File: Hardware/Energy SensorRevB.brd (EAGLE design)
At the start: 159 x 63 mm, 42 parts, among them IC1 7805, IC2 ATMega328p-pu, IC3 ld33v, Q1 16MHz, X1 MAINS IN, X2 MAINS OUT

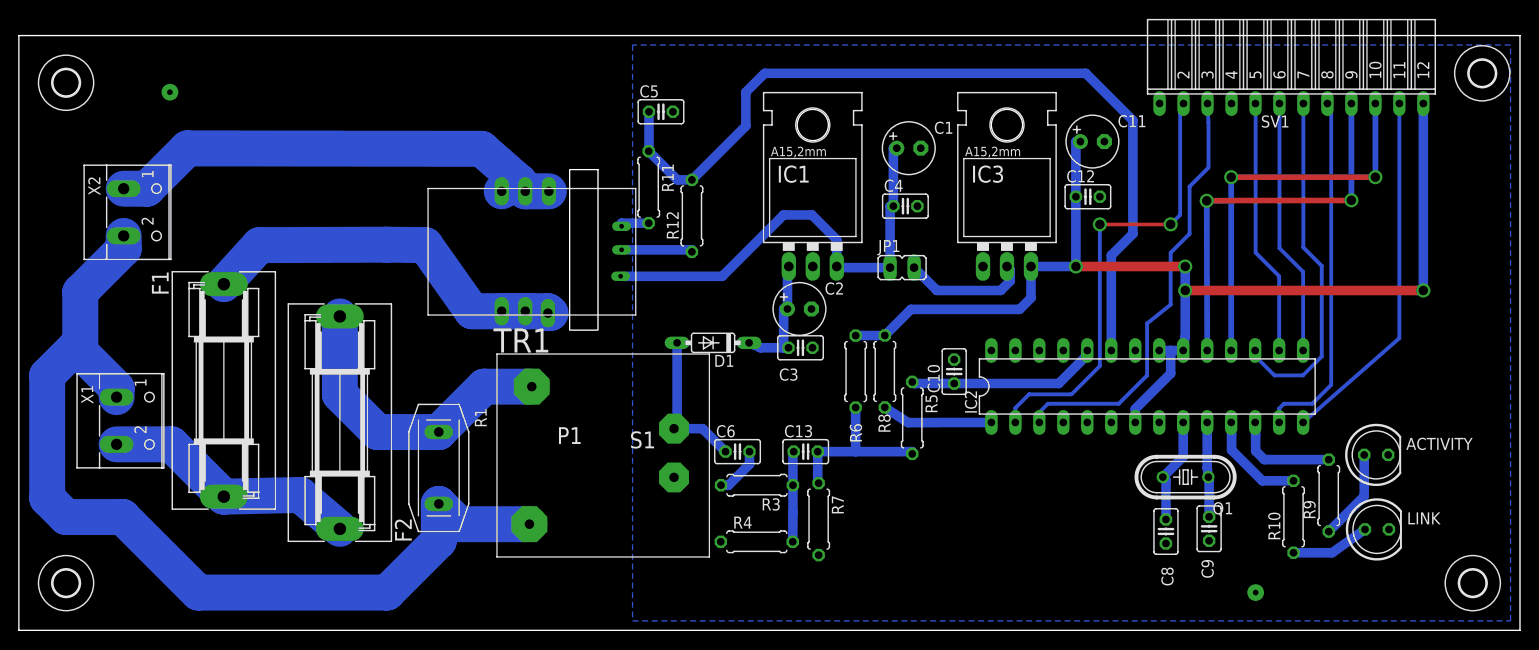
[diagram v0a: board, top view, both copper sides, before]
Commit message: updated scematic with new power regulator and 3.5mm jack connector for current meter
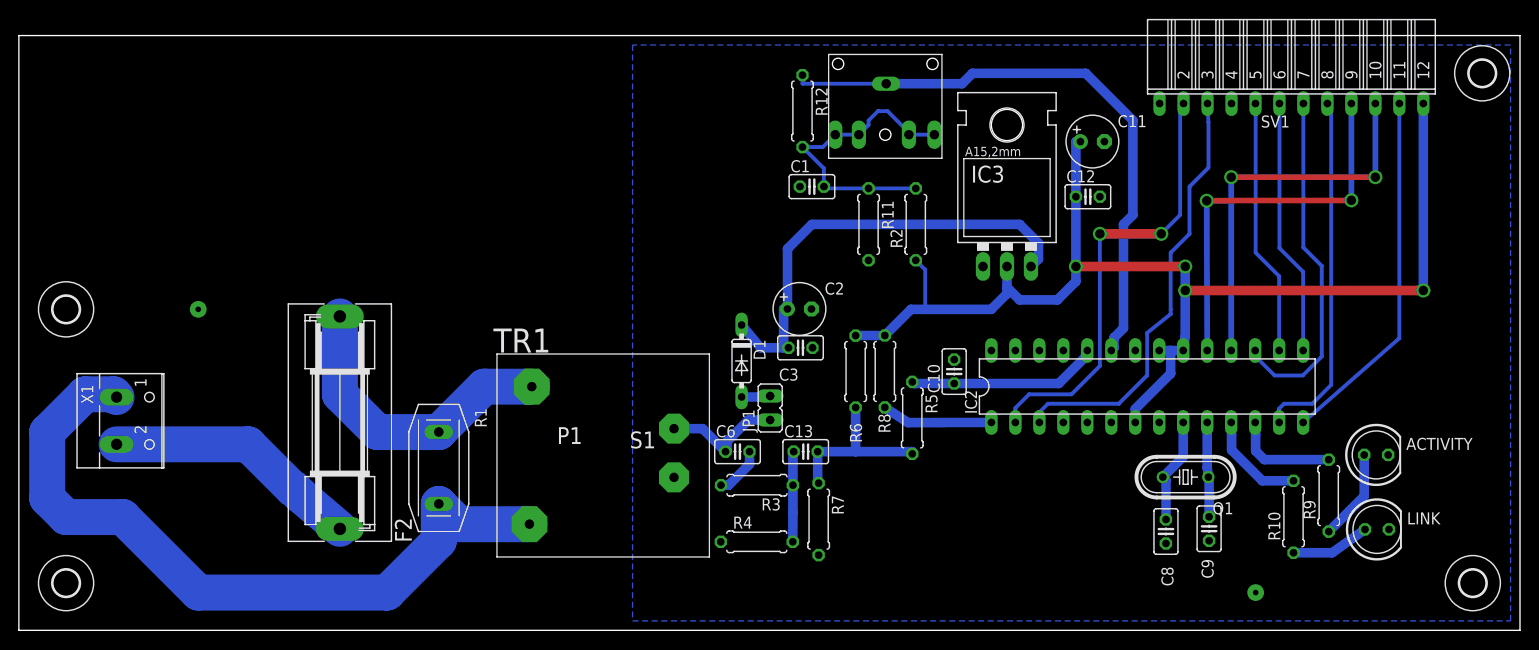
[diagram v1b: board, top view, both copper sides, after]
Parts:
- removed C4: 1n, rcl:C025-025X050
- removed C5: 1p, rcl:C025-025X050
- removed F1: 230V 10A, fuse:SH22,5A
- removed IC1: 7805, v-reg:78XXL
- removed X2: MAINS OUT, con-wago-500:W237-102
- added R2: 470k, rcl:0207/7
- C1: value 10u -> 1u; device rcl:E2,5-6 -> rcl:C025-025X050
- IC3: device v-reg:79XXL -> v-reg:317TL
- R11: value 56k -> 470k
- R12: value 68k -> 22R
- U$1: value CAS25-NP -> 3.5MMJACK; device CAS:CAS -> jack:3.5MMJACK
- moved U$1 28.0 mm to (91.8, 56.0), turned to 0 degrees
- moved H1 24.0 mm to (5.00, 34.0)
- moved R11 23.6 mm to (90.0, 43.0)
- moved JP1 20.4 mm to (79.6, 23.6), turned to 0 degrees
- moved R12 16.1 mm to (83.0, 55.0), turned to 270 degrees
- moved C1 11.0 mm to (84.0, 47.0)
- moved D1 3.58 mm to (76.5, 28.5), turned to 270 degrees
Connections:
- removed net +5V: C1.+, C4.1, IC1.OUT, JP1.1, U$1.13
- removed net N$11: R11.2, U$1.11
- removed net N$6: F1.1, U$1.1, U$1.2, U$1.3
- removed net N$8: U$1.10, U$1.8, U$1.9, X2.1
- new net N$1: C1.2, R11.1, R12.2, R2.2, U$1.2, U$1.3, U$1.4, U$1.5
- net +3V3: now also IC3.2, R2.1; no longer IC3.OUT
- net CURRENT_SENSE: now also R12.1, U$1.1; no longer C5.1, R11.1, R12.2
- net GND: now also C1.1, IC3.1, R11.2; no longer C1.-, C4.2, C5.2, IC1.GND, IC3.GND, R12.1, U$1.12
- net N$2: no longer X2.2
- net N$22: no longer F1.2
- net N$3: now also D1.A; no longer IC3.IN
- net N$5: now also JP1.1; no longer D1.A
- net N$7: now also IC3.3; no longer IC1.IN
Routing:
- net N$8: track 50.8 -> 0.00 mm
- net +5V: track 48.9 -> 0.00 mm
- net N$6: track 43.5 -> 0.00 mm
- net N$7: track 13.4 -> 48.3 mm
- net N$1: track 0.00 -> 31.9 mm
- net CURRENT_SENSE: track 90.9 -> 63.9 mm
- net N$2: track 100.8 -> 78.4 mm
- net N$3: track 13.3 -> 3.07 mm
- net +3V3: track 120.3 -> 128.5 mm
- net GND: track 7.86 -> 0.20 mm
- net N$11: track 3.20 -> 0.00 mm
- net N$5: track 15.9 -> 13.4 mm
- net RXD: track 48.1 -> 47.5 mm
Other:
- board text added: "Energy Meter Rev B."
- board text removed: "Energy Meter Rev A."

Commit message: Updated Rev B to reflect beneficial changes with Rev A pratical application, added noise suppressor to ARef. updated smoothing Ref Caps to match package. Added Additional Smoothing capacitors (due to unsteady supply) removed 5V Regulator. updated to new CT. Moved to smaller footprint. corrected Smoothing cap connected at incorrect place
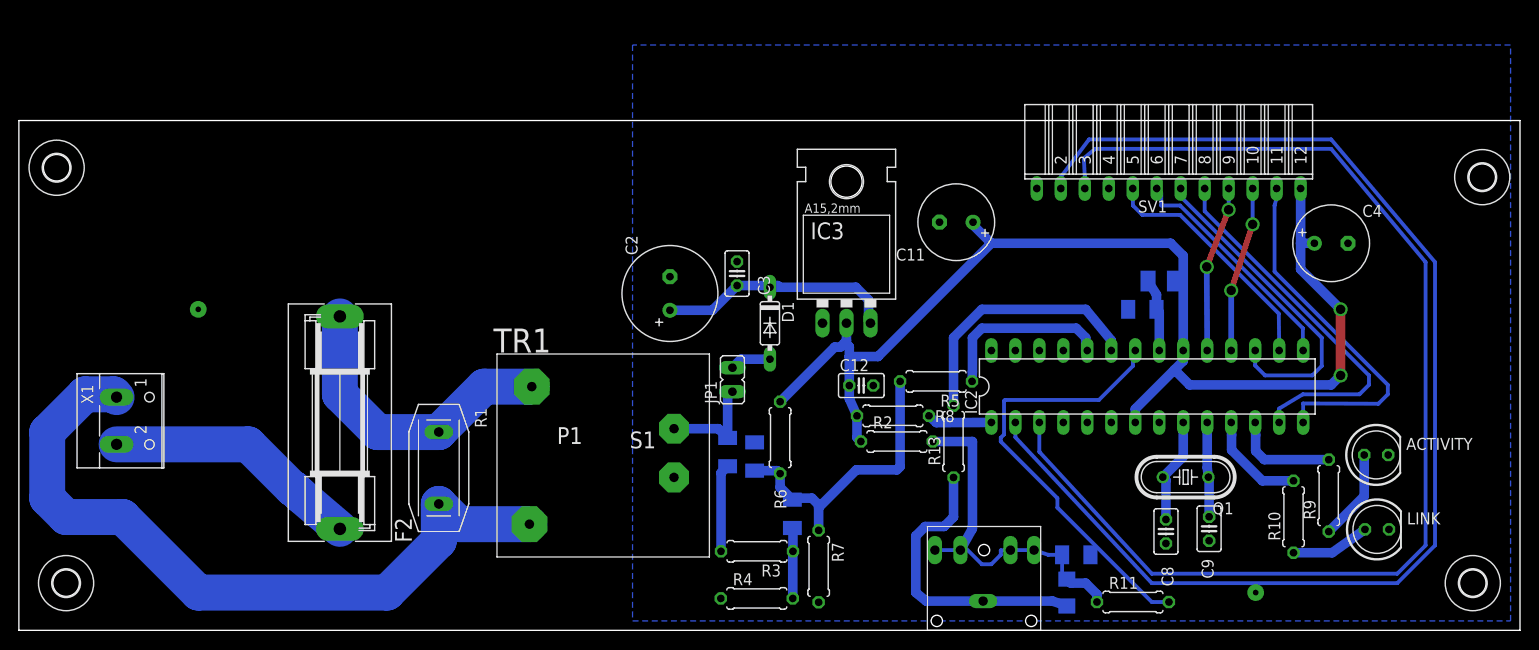
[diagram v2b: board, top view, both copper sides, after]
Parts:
- added C4: 10u, rcl:E3,5-8
- added C5: 100n, rcl:C1206K
- added L1: (no value), rcl:L3230M
- added R13: 1k, rcl:0207/7
- C1, C10: value 1u -> 10u; device rcl:C025-025X050 -> rcl:C1206K
- C11: device rcl:E2,5-6 -> rcl:E3,5-8
- C13, C6: device rcl:C025-025X050 -> rcl:C1206K
- C2: device rcl:E2,5-6 -> rcl:E3,5-10
- R12: device rcl:0207/7 -> rcl:R1206
- moved R12 58.2 mm to (111.0, 4.00), flipped to the bottom, turned to 90 degrees
- moved U$1 52.1 mm to (102.2, 5.00), turned to 180 degrees
- moved R11 48.8 mm to (118.0, 3.00), turned to 0 degrees
- moved C1 48.0 mm to (112.0, 8.00), flipped to the bottom
- moved C12 31.2 mm to (89.2, 25.9)
- moved R2 23.1 mm to (93.0, 20.0), turned to 0 degrees
- moved C10 23.0 mm to (77.9, 18.4), flipped to the bottom
- moved IC3 18.0 mm to (87.7, 36.4)
- moved C11 16.8 mm to (99.3, 43.2), turned to 180 degrees
- moved SV1 15.8 mm to (121.8, 46.8)
- moved H1 15.0 mm to (4.00, 49.0)
- moved C2 13.8 mm to (69.0, 35.7), turned to 90 degrees
- moved H4 11.0 mm to (155.0, 48.0)
- moved R6 10.6 mm to (80.6, 20.4)
- moved C3 10.3 mm to (76.1, 37.8), turned to 90 degrees
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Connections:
- new net N$6: R12.1, R13.1, U$1.1
- new net N$8: C5.1, IC2.21, L1.1
- net +3V3: now also C4.+, L1.2; no longer IC2.21
- net CURRENT_SENSE: now also R13.2; no longer R12.1, U$1.1
- net GND: now also C4.-, C5.2
- net N$10: now also C10.1
- net VSENSE: no longer C10.1
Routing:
- net RXD: track 47.5 -> 133.3 mm, vias 2 -> 0
- net TXD: track 45.8 -> 126.3 mm
- net GND: track 0.20 -> 47.0 mm
- net CURRENT_SENSE: track 63.9 -> 27.8 mm
- net N$6: track 0.00 -> 31.4 mm
- net MISO: track 41.4 -> 17.5 mm
- net SCK: track 41.4 -> 17.6 mm
- net N$7: track 48.3 -> 26.9 mm
- net N$10: track 18.4 -> 31.4 mm
- net N$8: track 0.00 -> 7.74 mm
- net N$1: track 31.9 -> 39.6 mm
- net N$16: track 11.8 -> 6.90 mm
- net N$4: track 5.29 -> 9.30 mm
- net N$5: track 13.4 -> 10.9 mm
- net MOSI: track 36.9 -> 34.5 mm
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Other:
- board size 159 x 63 mm -> 159 x 54 mm

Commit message: general tidying up before manufacture
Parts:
- L1: value (none) -> 10u
- moved H4 3.61 mm to (152.0, 50.0)
- moved H3 2.00 mm to (152.0, 5.00)
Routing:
- net CSN2: track 38.2 -> 34.8 mm
- net N$1: track 39.6 -> 38.0 mm
- net INT: track 39.8 -> 38.4 mm
- net CSN: track 24.8 -> 25.3 mm
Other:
- board size 159 x 54 mm -> 156 x 54 mm
- board text removed: "2015 Rev A"
- board text removed: "COMMS. MODULE"
- board text removed: "OUTPUT"
- board text removed: "Smart Home Energy Meter 2015"
